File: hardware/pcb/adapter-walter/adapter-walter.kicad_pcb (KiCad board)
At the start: 2 copper layers, 53.6 x 58.4 mm, 4 parts, among them U1 DPT_Walter

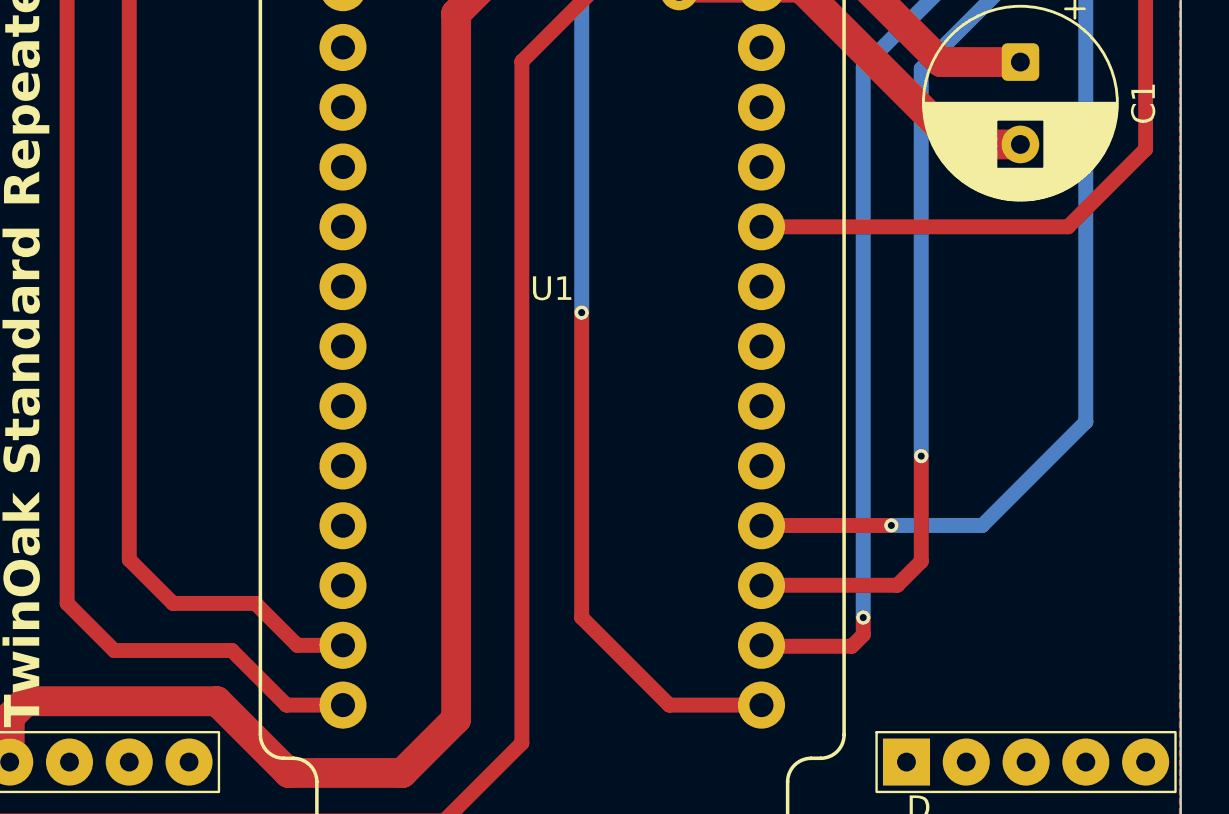
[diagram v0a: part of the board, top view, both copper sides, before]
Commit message: Cleanup. Added feedback prevention circuits to Walter adapter
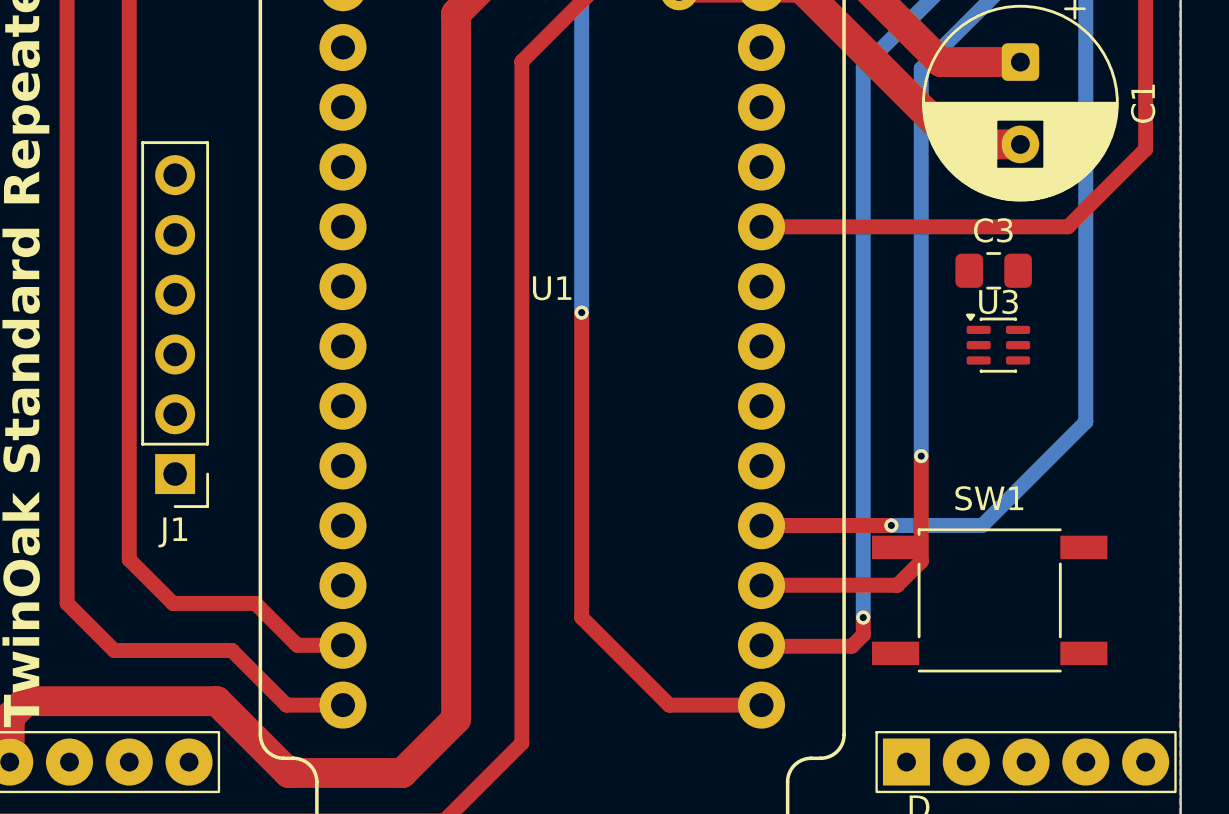
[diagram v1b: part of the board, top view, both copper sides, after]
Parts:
- added C3: 100n, Capacitor_SMD:C_0805_2012Metric_Pad1.18x1.45mm_HandSolder, F.Cu at (167.4, 86.9)
- added J1: UART0_RECOVERY, Connector_PinHeader_2.54mm:PinHeader_1x06_P2.54mm_Vertical, F.Cu at (132.6, 95.5)
- added SW1: RESET, TwinOak:SW_Push_Kinghelm_KH-6X6X5H-STM, F.Cu at (167.2, 100.9)
- added U3: LM66100, Package_TO_SOT_SMD:SOT-363_SC-70-6, F.Cu at (167.6, 90.0)
- C1: value C_Polarized -> 470u 16V
- C2: value C -> 10n
- U1: footprint walter:walter-socket -> TwinOak:walter-socket
- U2: value ~ -> Platform_LTE; footprint TwinOak platform footprints:platform-adapter-footprint -> TwinOak:platform-adapter-footprint
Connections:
- net IO1 renamed LORA_nRESET
- net IO2 renamed LORA_SWDCLK
- net IO3 renamed LORA_SWDIO
- net IO4 renamed LORA_PWR_KILL
- net IO5 renamed SPARE
- net IO6 renamed WALTER_TX
- net IO7 renamed WALTER_RX
- C1 pad 1: VCC -> WALTER_VIN
- C2 pad 1: VCC -> WALTER_VIN
- U1 pad 1: unconnected-(U1-~{RESET}-Pad1) -> WALTER_nRST
- U1 pad 2: unconnected-(U1-RX0/IO44-Pad2) -> WALTER_RX0
- U1 pad 28: VCC -> WALTER_VIN
- U1 pad 3: unconnected-(U1-TX0/IO43-Pad3) -> WALTER_TX0
- U1 pad 4: unconnected-(U1-IO0/~{3V3-EN}-Pad4) -> WALTER_IO0
- U2 pad 22: GND -> (no net)
- U2 pad 23: GND -> (no net)
- U2 pad 24: GND -> (no net)
- U2 pad 25: GND -> (no net)

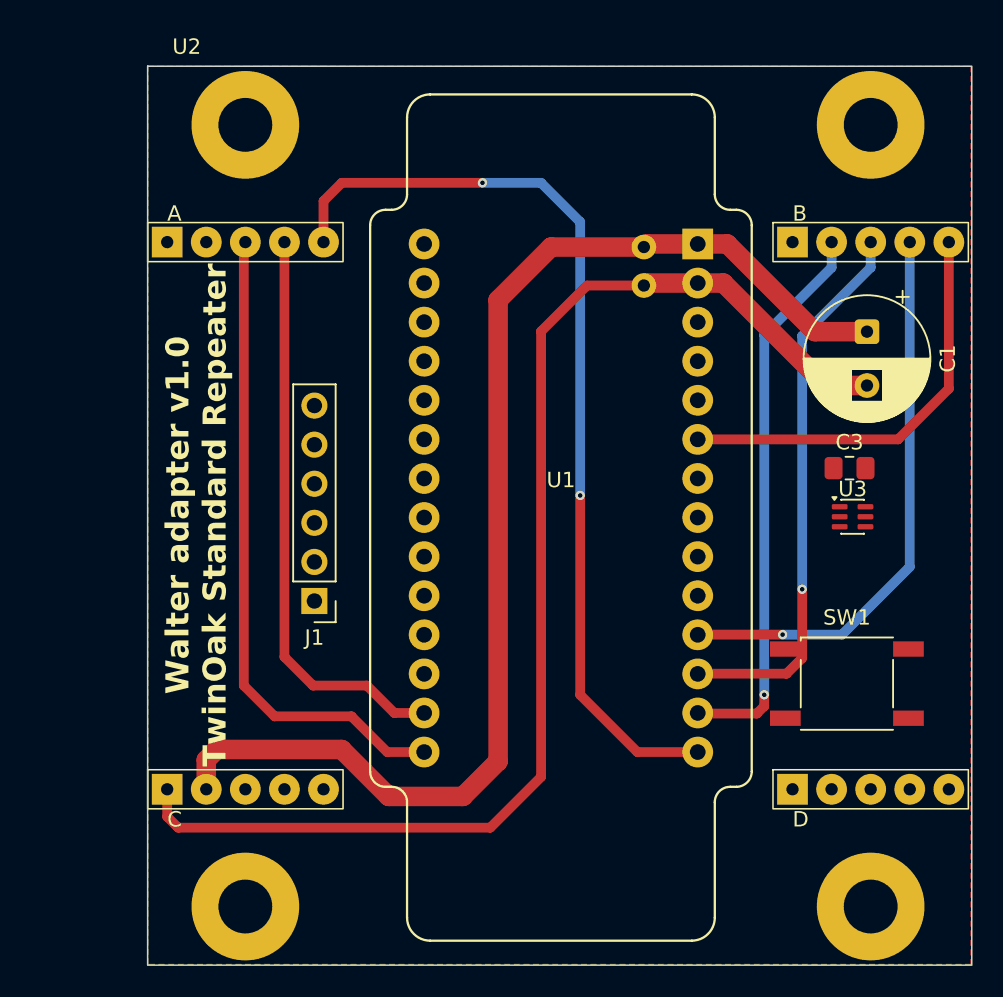
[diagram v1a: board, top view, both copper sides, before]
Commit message: Initial routing of walter - Not finished, missing polish
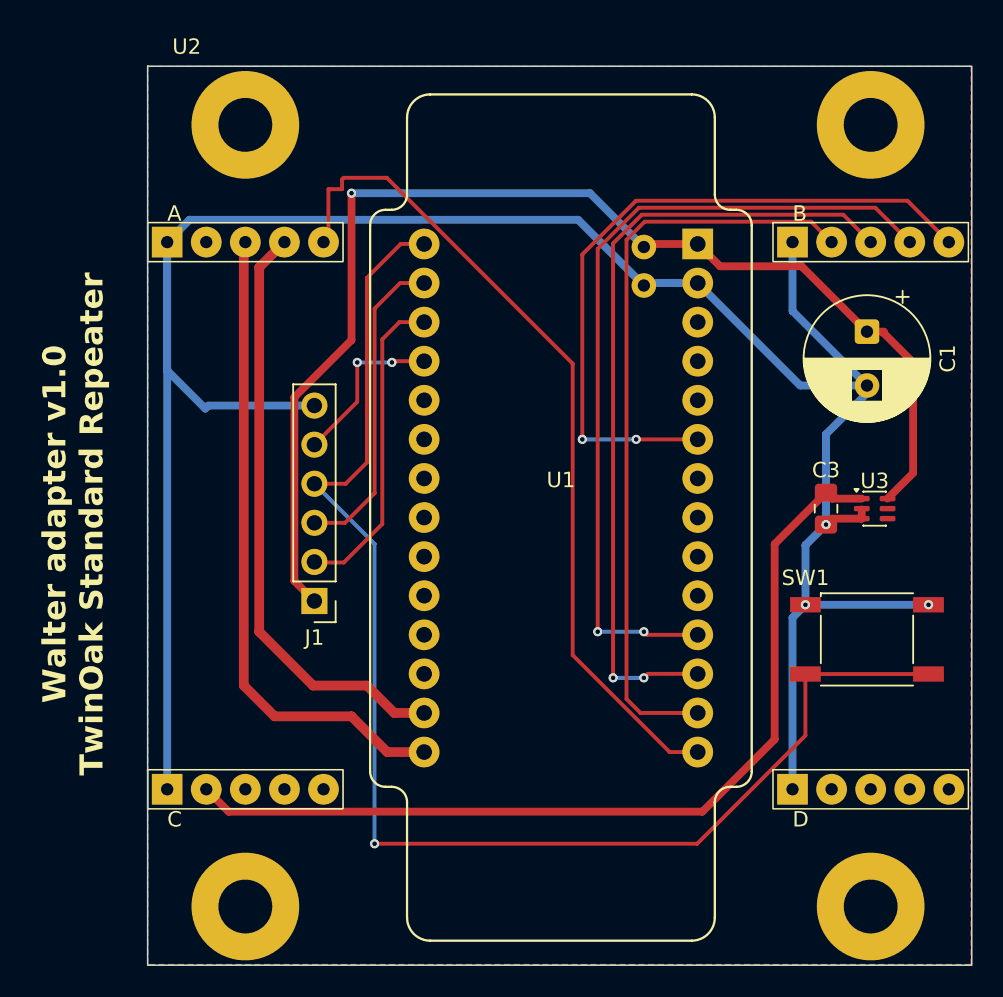
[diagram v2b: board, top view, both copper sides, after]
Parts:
- moved SW1 3.16 mm to (168.5, 98.0)
- moved C3 3.04 mm to (165.8, 89.5), turned to -90 degrees
- moved U3 1.53 mm to (169.0, 89.5)
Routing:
- net WALTER_nRST: track 0.00 -> 88.5 mm, vias 0 -> 1
- net WALTER_VIN: track 0.00 -> 79.4 mm, vias 0 -> 1
- net GND: track 81.9 -> 155.9 mm, vias 0 -> 3
- net VCC: track 81.2 -> 59.4 mm
- net WALTER_TX0: track 0.00 -> 20.6 mm
- net WALTER_RX0: track 0.00 -> 20.6 mm
- net WALTER_RX: track 27.2 -> 45.9 mm, vias 0 -> 2
- net WALTER_TX: track 36.7 -> 53.8 mm, vias 1 -> 2
- net SPARE: track 36.1 -> 52.1 mm, vias 1 -> 2
- net LORA_PWR_KILL: track 36.5 -> 49.2 mm, vias 1 -> 0
- net WALTER_IO0: track 0.00 -> 10.9 mm, vias 0 -> 2
- net LORA_SWDIO: track 60.8 -> 54.8 mm, vias 2 -> 0
- net LORA_SWDCLK: track 37.5 -> 38.9 mm

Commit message: Minor adjustments to PCBs
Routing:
- net GND: track 155.9 -> 169.2 mm
- net LORA_SWDIO: track 54.8 -> 61.6 mm
- net LORA_PWR_KILL: track 49.2 -> 53.4 mm
- net WALTER_TX: track 53.8 -> 57.2 mm
- net SPARE: track 52.1 -> 55.6 mm
- net WALTER_RX: track 45.9 -> 48.6 mm
- net LORA_SWDCLK: track 38.9 -> 41.4 mm
- net VCC: track 59.4 -> 61.8 mm
- net WALTER_VIN: track 79.4 -> 81.8 mm
- net LORA_nRESET: track 42.4 -> 44.3 mm
- net WALTER_nRST: track 88.5 -> 87.1 mm
- net WALTER_IO0: track 10.9 -> 12.1 mm
- added copper zone on B.Cu, net GND

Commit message: Final PCB adjuments to rev 1.1
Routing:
- net GND: vias 3 -> 54
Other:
- board text added: "USB-C THIS END"

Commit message: Last pre-production updates
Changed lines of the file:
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@@
+			)
+		)
+		(property "FT Rotation Offset" "90"
+			(at 0 0 0)
+			(unlocked yes)
+			(layer "F.Fab")
+			(hide yes)
+			(effects
+				(font
+					(size 1 1)
+					(thickness 0.15)
+				)
 			)
 		)
@@
 		(property "Value" "UART0_RECOVERY"
 			(at 2.286 6.604 90)
-			(layer "F.Fab")
+			(layer "F.SilkS")
 			(effects
 				(font
@@
 		(property "Value" "RESET"
 			(at 0 4 0)
-			(layer "F.Fab")
-			(effects
-				(font
+			(layer "F.SilkS")
+			(effects
+				(font

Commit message: Parts ordered!
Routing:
- net GND: track 169.2 -> 171.0 mm
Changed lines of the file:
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@@
 			)
 		)
-		(property "MPN" "Panasonic 16SEPG470M (OS-CON)"
+		(property "MPN" "Honor Elec RYHT16V470UF8*11 (alt. Panasonic 16SEPG470M)"
+			(at 0 0 270)
+			(unlocked yes)
+			(layer "F.Fab")
+			(hide yes)
+			(effects
+				(font
+					(size 1 1)
+					(thickness 0.15)
+				)
+			)
+		)
+		(property "LCSC Part #" "C48970577"
 			(at 0 0 270)
 			(unlocked yes)
@@
 	)
 	(segment
-		(start 166.225 90.15)
-		(end 165.8375 90.5375)
+		(start 166.7645 90.5375)
+		(end 167.152 90.15)
 		(width 0.508)
 		(layer "F.Cu")
@@
 	)
 	(segment
-		(start 168.1625 90.15)
-		(end 166.225 90.15)
+		(start 167.152 90.15)
+		(end 168.1625 90.15)
+		(width 0.508)
+		(layer "F.Cu")
+		(net "GND")
+	)
+	(segment
+		(start 165.8375 90.5375)
+		(end 166.7645 90.5375)
 		(width 0.508)
 		(layer "F.Cu")
@@
 		(net "GND")
 	)
+	(segment
+		(start 164.2245 90.5375)
+		(end 165.8375 90.5375)
+		(width 0.508)
+		(layer "F.Cu")
+		(net "GND")
+	)
 	(via
 		(at 163.576 116.84)
@@
 	)
 	(via
-		(at 165.8375 90.5375)
+		(at 164.2245 90.5375)
 		(size 0.6)
 		(drill 0.3)
@@
 	)
 	(via
-		(at 164.5 95.75)
+		(at 164.5 94.234)
 		(size 0.6)
 		(drill 0.3)
@@
 	)
 	(via
-		(at 172.5 95.75)
+		(at 172.5 94.234)
 		(size 0.6)
 		(drill 0.3)
@@
 	)
 	(segment
+		(start 164.5 94.234)
+		(end 164.5 95.75)
+		(width 0.508)
+		(layer "B.Cu")
+		(net "GND")
+	)
+	(segment
 		(start 125.5 83)
 		(end 125.696 82.804)
@@
 	)
 	(segment
-		(start 168.5 81.5)
-		(end 168.5 82)
+		(start 164.5 91.875)
+		(end 164.2245 91.5995)
 		(width 0.508)
 		(layer "B.Cu")
@@
 	(segment
 		(start 168.5 82)
-		(end 165.8375 84.6625)
+		(end 168.5 81.5)
+		(width 0.508)
+		(layer "B.Cu")
+		(net "GND")
+	)
+	(segment
+		(start 165.8375 84.6625)
+		(end 168.5 82)
 		(width 0.508)
 		(layer "B.Cu")
@@
 	)
 	(segment
-		(start 163.66 96.59)
-		(end 164.5 95.75)
-		(width 0.508)
-		(layer "B.Cu")
-		(net "GND")
-	)
-	(segment
 		(start 163.66 72.18)
 		(end 163.66 81)
@@
 	)
 	(segment
-		(start 164.5 95.75)
+		(start 164.5 94.234)
 		(end 164.5 91.875)
 		(width 0.508)
@@
 	)
 	(segment
-		(start 163.66 107.74)
-		(end 163.66 96.59)
+		(start 164.2245 91.5995)
+		(end 164.2245 90.5375)
 		(width 0.508)
 		(layer "B.Cu")
@@
 	)
 	(segment
+		(start 164.5 95.75)
+		(end 163.66 96.59)
+		(width 0.508)
+		(layer "B.Cu")
+		(net "GND")
+	)
+	(segment
+		(start 164.2245 90.2835)
+		(end 165.8375 88.6705)
+		(width 0.508)
+		(layer "B.Cu")
+		(net "GND")
+	)
+	(segment
 		(start 163.66 81)
 		(end 163.66 74.84)
@@
 	)
 	(segment
-		(start 165.8375 84.6625)
-		(end 165.8375 90.5375)
-		(width 0.508)
-		(layer "B.Cu")
-		(net "GND")
-	)
-	(segment
 		(start 123.02 80.52)
 		(end 125.5 83)
@@
 	)
 	(segment
-		(start 164.5 91.875)
-		(end 165.8375 90.5375)
+		(start 172.5 94.234)
+		(end 164.5 94.234)
+		(width 0.508)
+		(layer "B.Cu")
+		(net "GND")
+	)
+	(segment
+		(start 165.8375 88.6705)
+		(end 165.8375 84.6625)
 		(width 0.508)
 		(layer "B.Cu")
@@
 	)
 	(segment
+		(start 163.66 96.59)
+		(end 163.66 107.74)
+		(width 0.508)
+		(layer "B.Cu")
+		(net "GND")
+	)
+	(segment
 		(start 125.696 82.804)
 		(end 132.588 82.804)
@@
 	)
 	(segment
-		(start 164.5 95.75)
-		(end 172.5 95.75)
-		(width 0.508)
-		(layer "B.Cu")
+		(start 164.2245 90.5375)
+		(end 164.2245 90.2835)
+		(width 0.508)
+		(layer "B.Cu")
